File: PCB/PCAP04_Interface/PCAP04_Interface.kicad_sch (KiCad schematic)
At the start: 23 parts, among them J1 Conn_01x04, J2 43045-2022, J3 MEM2067-02-180-00-A, U1 PCAP_04-eva-board, U2 ESP-WROOM-32-DEVBOARD

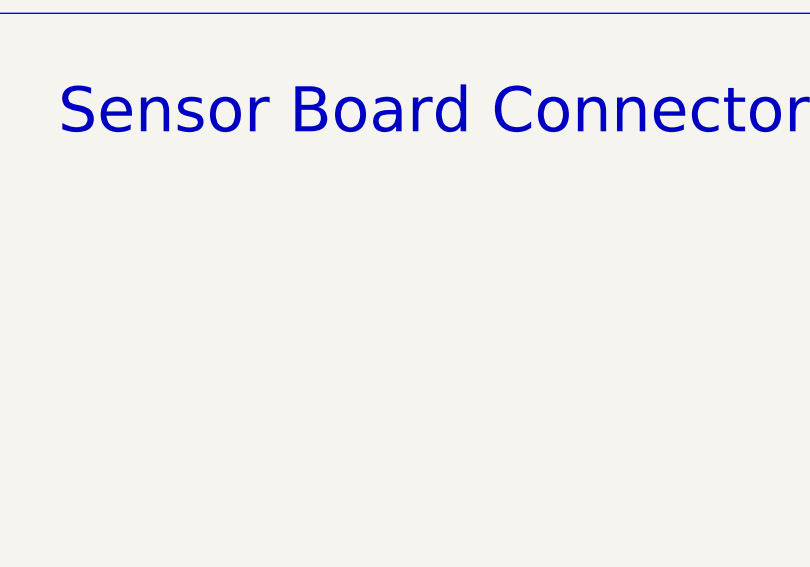
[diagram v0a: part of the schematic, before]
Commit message: Added breakout for C1.5 and C2.5, updated readme
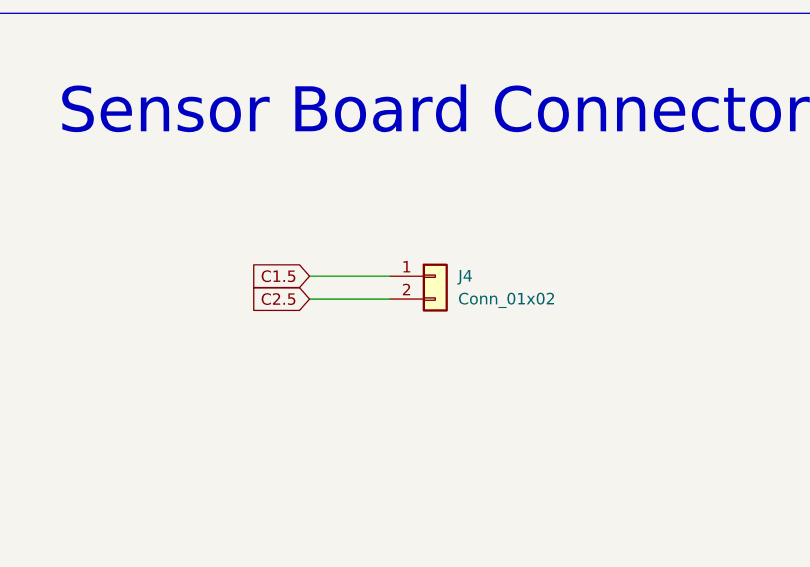
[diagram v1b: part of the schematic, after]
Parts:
- added J4: Conn_01x02, Connector_PinSocket_2.54mm:PinSocket_1x02_P2.54mm_Vertical, symbol Connector_Generic:Conn_01x02
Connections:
- net C1.5: now also J4.1 (Pin_1)
- net C2.5: now also J4.2 (Pin_2)
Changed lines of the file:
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@@
+    (stroke (width 0) (type default) (color 0 0 0 0))
+  )
+  (wire (pts (xy 196.85 180.34) (xy 205.74 180.34))
     (stroke (width 0) (type default) (color 0 0 0 0))
   )
@@
   )
   (polyline (pts (xy 342.9 194.31) (xy 344.17 194.31))
+    (stroke (width 0) (type default) (color 0 0 0 0))
+  )
+  (wire (pts (xy 196.85 177.8) (xy 205.74 177.8))
     (stroke (width 0) (type default) (color 0 0 0 0))
   )
@@
     )
   )
+  (global_label "C1.5" (shape input) (at 196.85 177.8 180) (fields_autoplaced)
+    (effects (font (size 1.27 1.27)) (justify right))
+    (property "Intersheet References" "${INTERSHEET_REFS}" (id 0) (at 190.1431 177.7206 0)
+      (effects (font (size 1.27 1.27)) (justify right) hide)
+    )
+  )
   (global_label "PR1-SENSE" (shape input) (at 318.77 67.31 180) (fields_autoplaced)
     (effects (font (size 1.27 1.27)) (justify right))
@@
     (effects (font (size 1.27 1.27)) (justify right))
     (property "Intersheet References" "${INTERSHEET_REFS}" (id 0) (at 174.1774 116.7606 0)
+      (effects (font (size 1.27 1.27)) (justify right) hide)
+    )
+  )
+  (global_label "C2.5" (shape input) (at 196.85 180.34 180) (fields_autoplaced)
+    (effects (font (size 1.27 1.27)) (justify right))
+    (property "Intersheet References" "${INTERSHEET_REFS}" (id 0) (at 190.1431 180.2606 0)
       (effects (font (size 1.27 1.27)) (justify right) hide)
     )
@@
     (pin "1")
   )
+  (symbol (lib_id "Connector_Generic:Conn_01x02") (at 210.82 177.8 0) (unit 1)
+    (in_bom yes) (on_board yes) (fields_autoplaced)
+    (property "Reference" "J4" (id 0) (at 213.36 177.7999 0)
+      (effects (font (size 1.27 1.27)) (justify left))
+    )
+    (property "Value" "Conn_01x02" (id 1) (at 213.36 180.3399 0)
+      (effects (font (size 1.27 1.27)) (justify left))
+    )
+    (property "Footprint" "Connector_PinSocket_2.54mm:PinSocket_1x02_P2.54mm_Vertical" (id 2) (at 210.82 177.8 0)
+      (effects (font (size 1.27 1.27)) hide)
+    )
+    (property "Datasheet" "~" (id 3) (at 210.82 177.8 0)
+      (effects (font (size 1.27 1.27)) hide)
+    )
+    (pin "1")
+    (pin "2")
+  )
   (sheet (at 97.79 41.91) (size 17.78 24.13) (fields_autoplaced)
     (stroke (width 0.1524) (type solid) (color 0 0 0 0))
@@
       (reference "J3") (unit 1) (value "MEM2067-02-180-00-A") (footprint "FootrpintLib:MEM20670218000A")
     )
+    (path "/ffd4827b-4efc-440f-9990-5046587a952b"
+      (reference "J4") (unit 1) (value "Conn_01x02") (footprint "Connector_PinSocket_2.54mm:PinSocket_1x02_P2.54mm_Vertical")
+    )
     (path "/2e2c637e-8c37-4a2f-b5da-2da83c8b3c56"

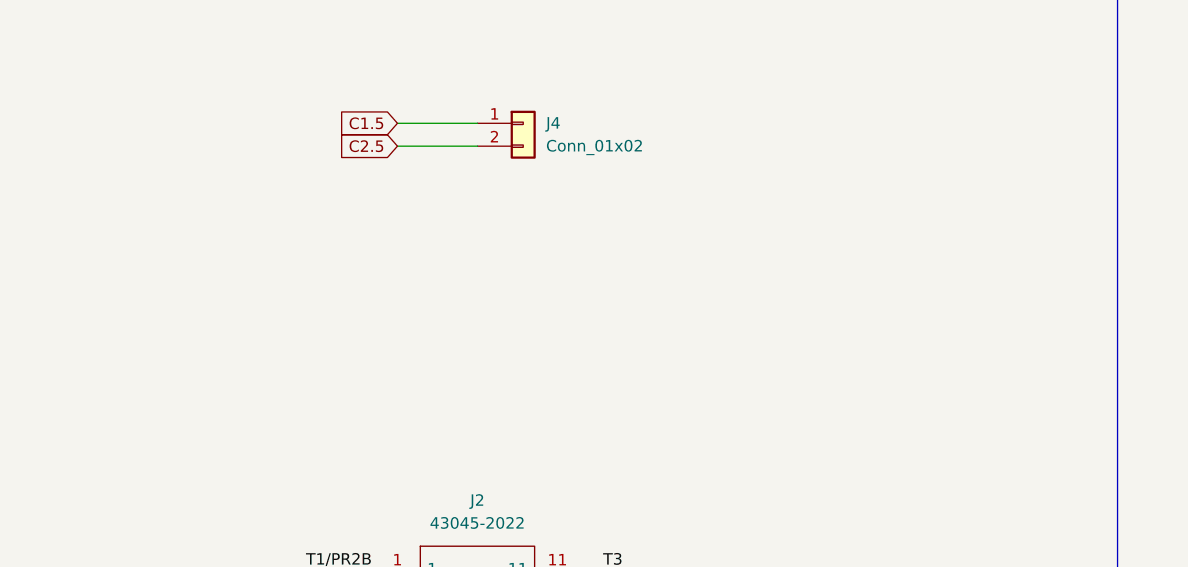
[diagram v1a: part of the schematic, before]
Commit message: Created PlatformIO-based project
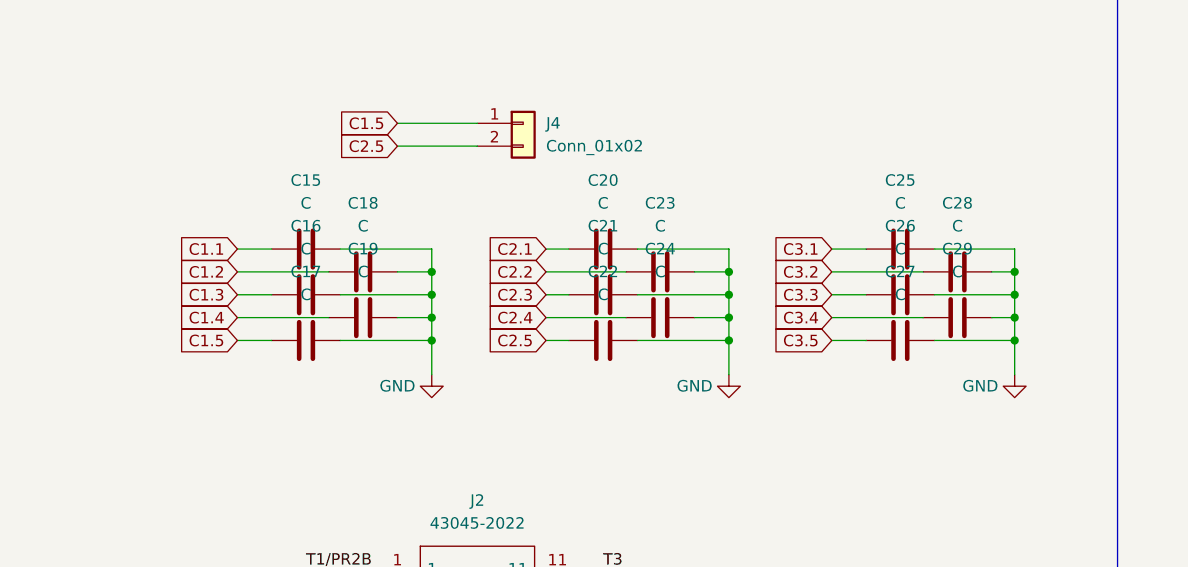
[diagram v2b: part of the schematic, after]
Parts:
- added C15, C16, C17, C18, C19, C20, C21, C22, C23, C24, C25, C26, C27, C28, C29: C, Capacitor_SMD:C_0603_1608Metric_Pad1.08x0.95mm_HandSolder, symbol Device:C
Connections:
- net C1.1: now also C15.2
- net C1.2: now also C18.2
- net C1.3: now also C16.2
- net C1.4: now also C19.2
- net C1.5: now also C17.2
- net C2.1: now also C20.2
- net C2.2: now also C23.2
- net C2.3: now also C21.2
- net C2.4: now also C24.2
- net C2.5: now also C22.2
- net C3.1: now also C25.2
- net C3.2: now also C28.2
- net C3.3: now also C26.2
- net C3.4: now also C29.2
- net C3.5: now also C27.2
- net GND: now also C15.1, C16.1, C17.1, C18.1, C19.1, C20.1, C21.1, C22.1, C23.1, C24.1, C25.1, C26.1, C27.1, C28.1, C29.1
